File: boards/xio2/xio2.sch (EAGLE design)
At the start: 352 parts, among them J1 12401598E4#2A, Q1 BSS138, Q2 BSS138, Q3 BC817-16LT3G, Q4 BC817-16LT3G, Y2 FA-238 25.0000MB-K3

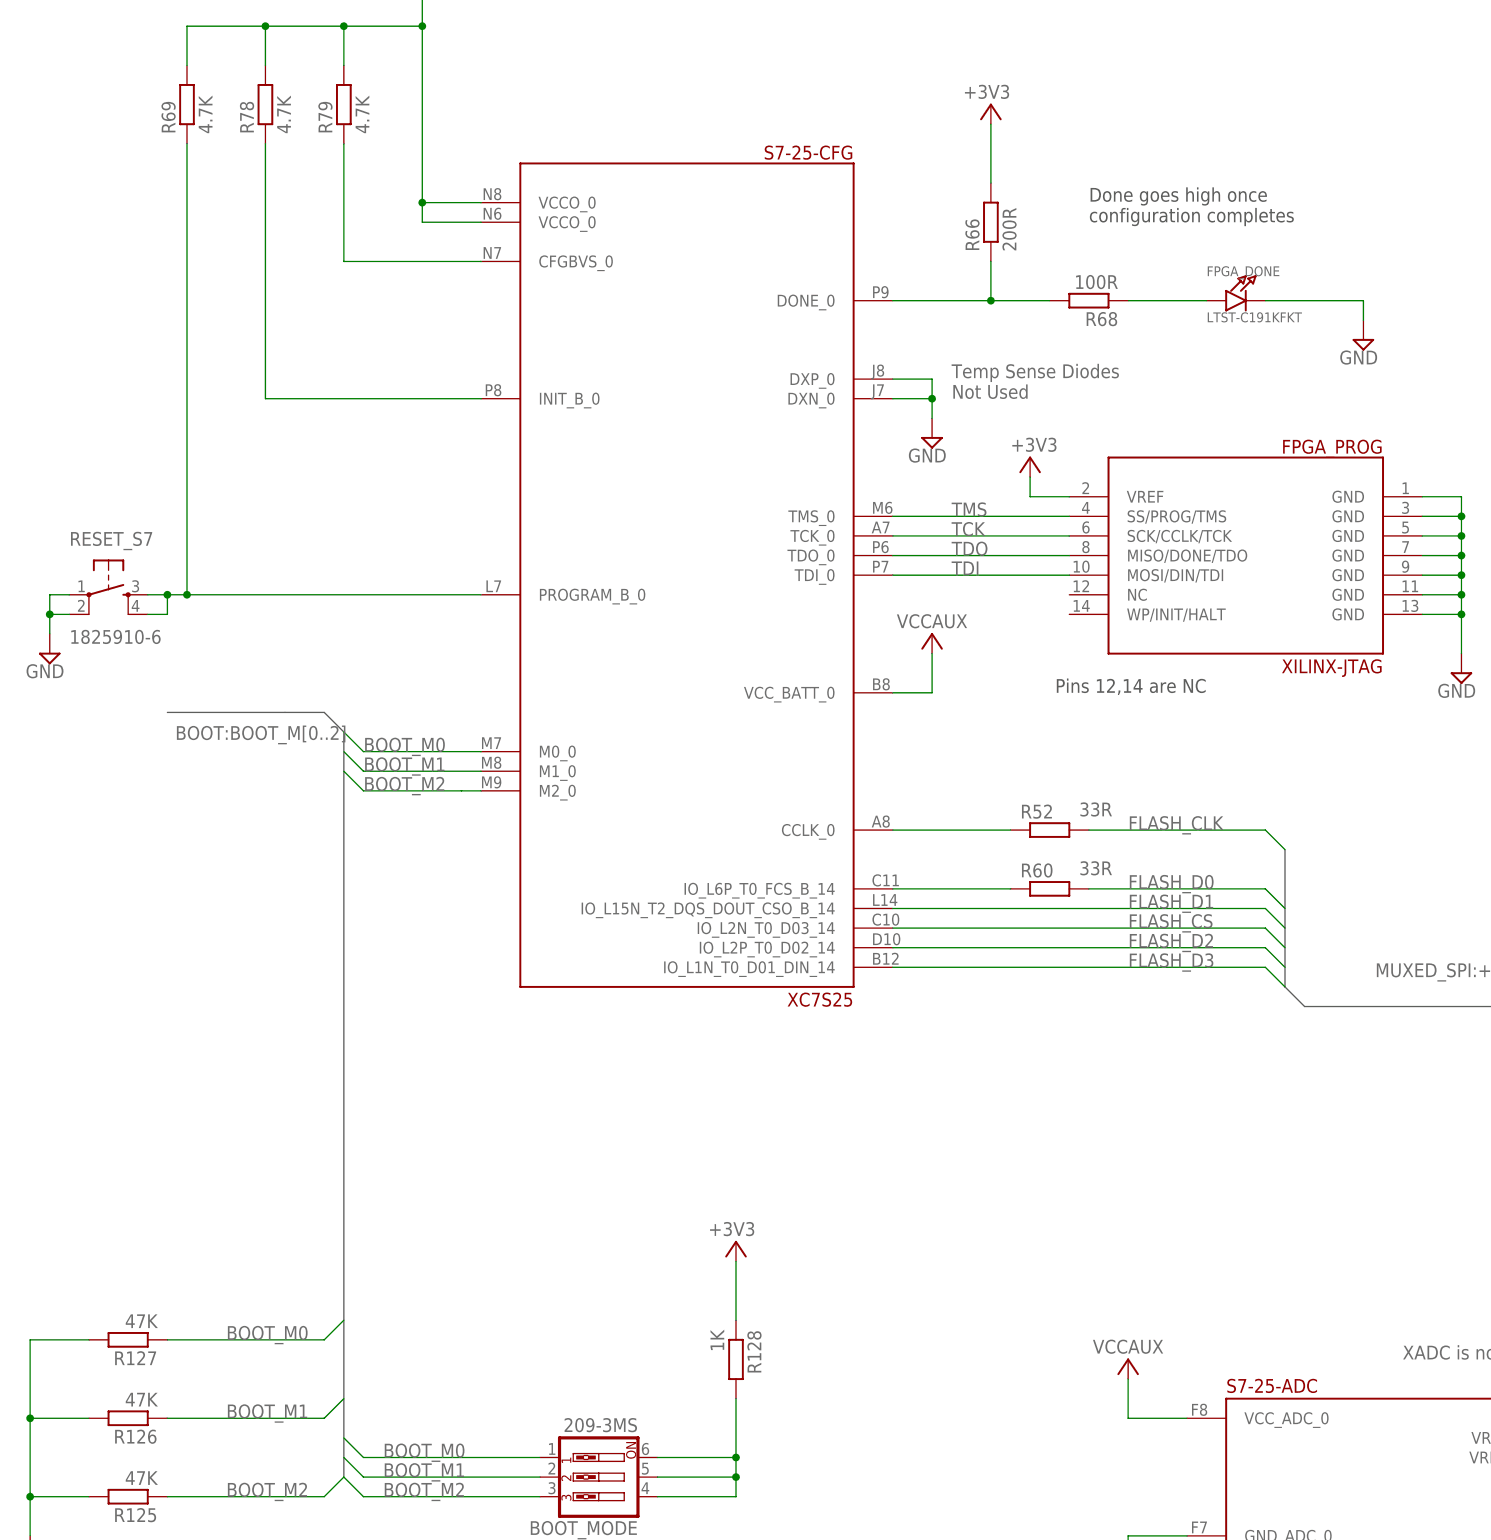
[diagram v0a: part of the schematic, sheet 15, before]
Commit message: All pins checked vs data sheets All parts provisionally given USE attributes
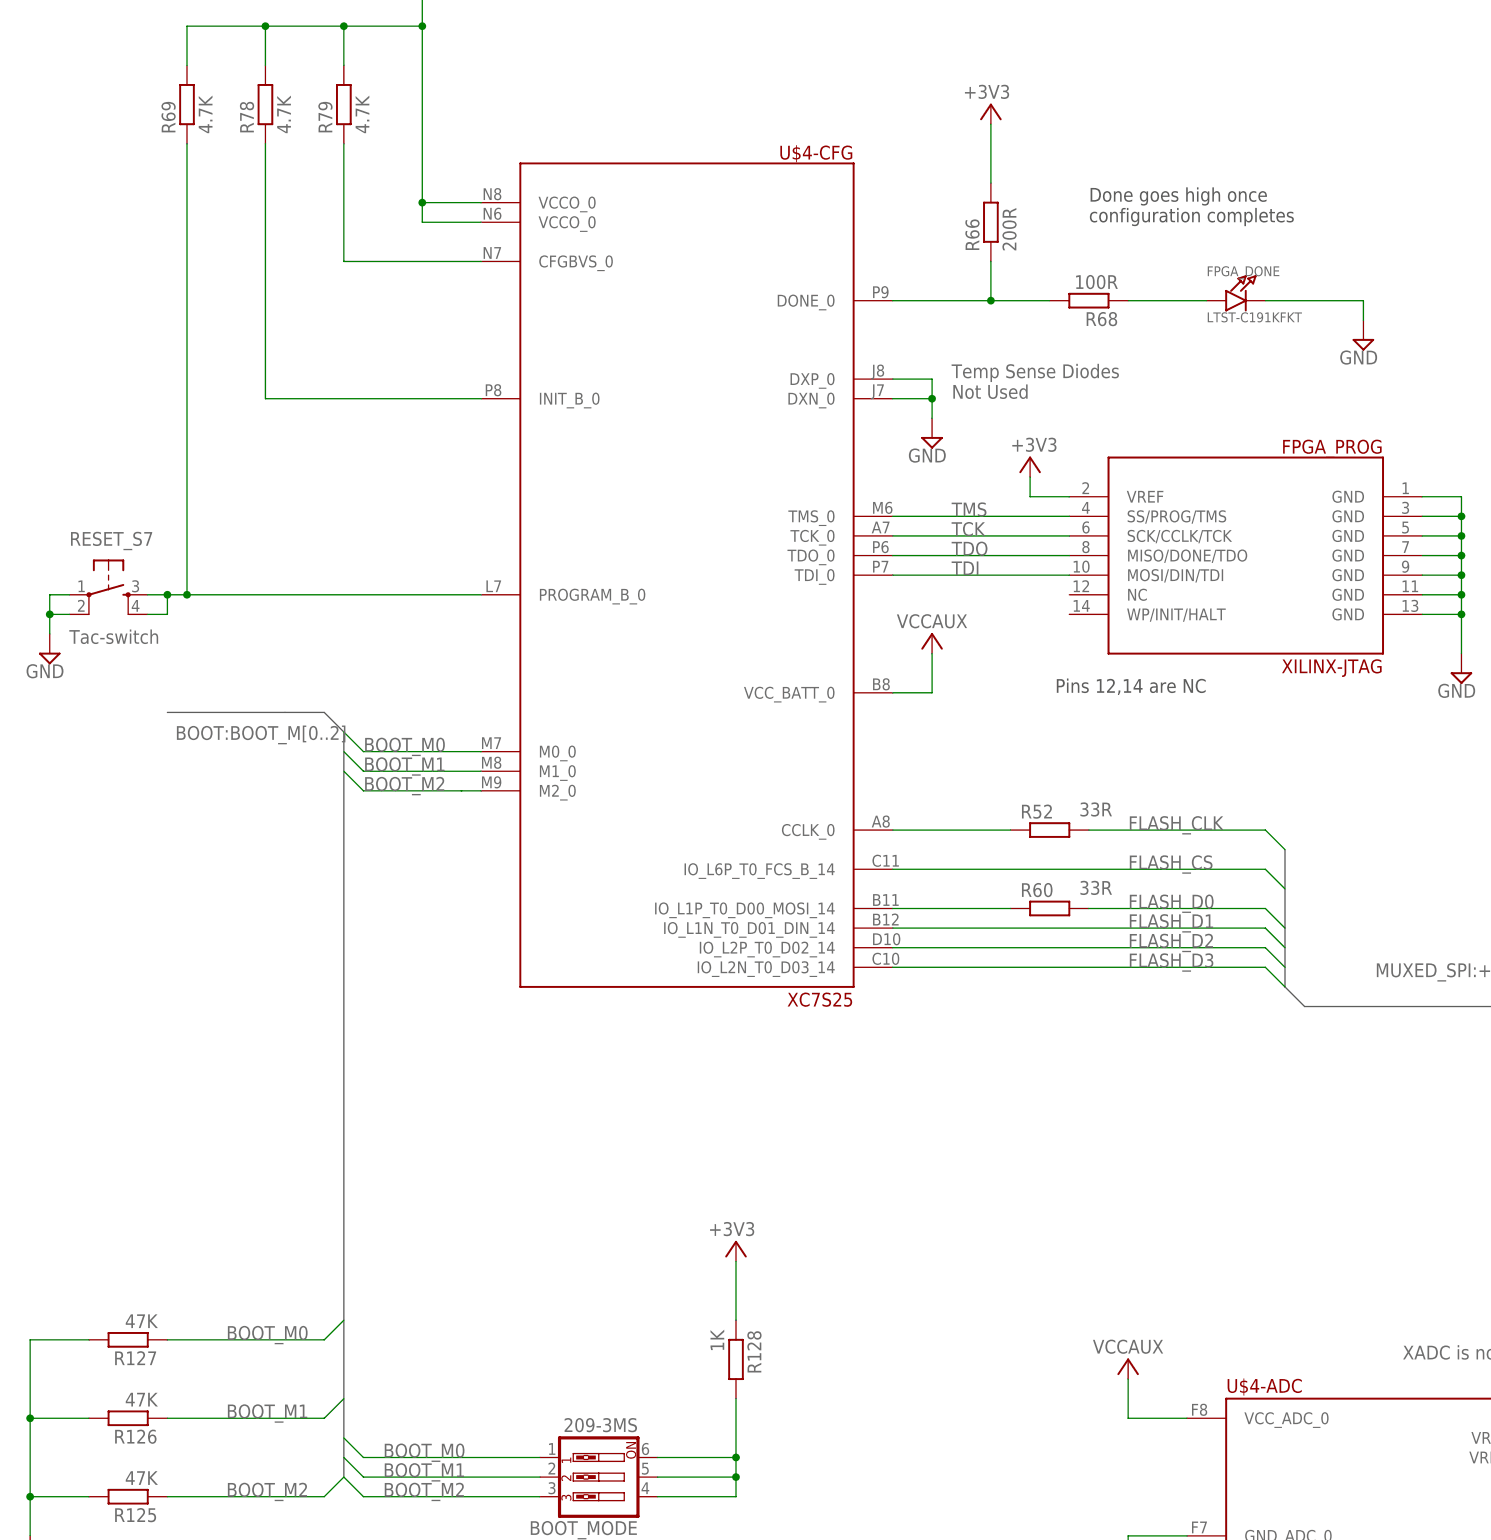
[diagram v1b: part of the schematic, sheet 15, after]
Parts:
- removed LVL_CLK, LVL_RD4, LVL_RD5, LVL_RW: 74LVCH1T45GW,125, sjg-logic:74LVC1T45GW,125
- added R58: 1K, rcl:R-EU_R0201
- added U$5, U$6, U$7, U$8: 74LVC1T45GWSOT866, sjg-logic:74LVC1T45GWSOT866
- A_MUX: USE (none) -> TS3A27518EPWR
- BOOT_MODE: USE (none) -> 209-3MS
- C100, C25, C57, C60, C61, C62, C63, C64, C65, C66, C67, C68, C69, C70, C71, C72, C88, C96: USE (none) -> GRM033R61A104ME15D
- C101, C73, C77: USE (none) -> GRM21BR60J107ME15L
- C102, C59, C74, C75, C76, C78, C79, C82: USE (none) -> GRM155R60J475ME87D
- C104, C30, C36, C47, C48, C49, C50, C51, C83, C84, C85, C86: USE (none) -> GRM033R60J474KE90D
- C109, C110: device rcl:C-EUC0603 -> rcl:C-EUC0805; USE (none) -> CL21A226MOCLRNC
- C111: USE (none) -> CL05B103KA5NNNC
- C112: USE (none) -> CL05B392KB5NNNC
- C35: value 0.01uF -> 0.1uF; USE (none) -> GRM033R61A104ME15D
- C52: USE (none) -> GRM21BR60J476ME15L
- C97: USE (none) -> GRM033R60J105MEA2D
- CARTRIDGE: USE (none) -> 5650118-1
- EXPANSION, EXP_POWER: NOSTUFF (none) -> true
- FPGA_1_0: USE (none) -> TLV62095RGTR
- FPGA_CFG: USE (none) -> MX25L3206EM2I-12G
- FPGA_DONE: UE (none) -> LTST-C191KFKT
- FPGA_PROG: USE (none) -> SBH21-NBPN-D07-ST-BK
- J1: USE (none) -> 12401598E4#2A
- L1: USE (none) -> ASPI-0530LR-1R5M-T2
- LD_0ACT, LD_1ACT, LD_2ACT, LD_3ACT, LD_4ACT: USE (none) -> 150060RS75000
- LD_0P, LD_1P, LD_2P, LD_3P, LD_4P: USE (none) -> SML-D12D1WT86
- LD_7DBG0, LD_7DBG1, LD_7DBG2: USE (none) -> ASMT-RA45-AP932
- LD_AUX, LD_INT, LD_V33: USE (none) -> LTST-S270GKT
- LVL_AHI, LVL_ALO, LVL_D: USE (none) -> SN74LVC8T245PWR
- MUX-HI, MUX-LO: USE (none) -> QS3VH257S1G
- OSC1: value ASEMB-50.000MHZ-LC-T -> 50 MHz oscillator; USE (none) -> SIT8008BI-23-33S-50.000000G
- Q3, Q4: USE (none) -> BC817-16LT3G
- R101, R104, R107, R87, R98: value 55R -> 59R; USE (none) -> RMCF0402FT59R0
- R102, R105, R108, R109, R110, R111, R94, R99: USE (none) -> RMCF0402JT130R
- R112: value 60R -> 59R; USE (none) -> RMCF0402FT59R0
- R113, R114, R115, R116, R117, R118: USE (none) -> RMCF0201FT49R9
- R125, R126, R127: USE (none) -> RMCF0402JT47K0
- R128: USE (none) -> RMCF0201JT1K00
- R129: USE (none) -> ERJ-2RKF4993X
- R130: USE (none) -> RMCF0402FT40K2
- R131: USE (none) -> RMCF0402JT160K
- R52, R60, R73, R74, R75: USE (none) -> RMCF0201JT33R0
- R54, R55, R57: USE (none) -> RC0603F242CS
- R66: USE (none) -> ERJ-1GNJ201C
- R67, R77: USE (none) -> RMCF0402JT150R
- R68: device rcl:R-EU_R0201 -> rcl:R-EU_R0402; USE (none) -> ERJ-2GEJ101X
- R69, R70, R71, R78, R79: USE (none) -> RC0603J472CS
- R76, R80: USE (none) -> RMCF0402JT330R
- RESET_S7: value 1825910-6 -> Tac-switch; USE (none) -> 1825910-6
- U$4: USE (none) -> XC7S25-2FTGB196I
- VREG_18: USE (none) -> TPS62087RLTR
- VREG_33: USE (none) -> LM21212MHX-2/NOPB
- XIO: USE (none) -> STM32H743XIH6
- renumbered S7-25 to U$4
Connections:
- removed net N$52: R60.1, U$4-CFG.IO_L6P_T0_FCS_B_14@C11
- new net N$3: R60.1, U$4-CFG.IO_L1P_T0_D00_MOSI_14@B11
- new net N$5: OSC1.INH, R58.2
- net +3V3: now also R58.1, U$5.DIR@5, U$5.VCCA@1, U$6.DIR@5, U$6.VCCA@1, U$7.VCCB@6, U$8.VCCB@6; no longer LVL_CLK.DIR@5, LVL_CLK.VCCA@1, LVL_RD4.VCCB@6, LVL_RD5.VCCB@6, LVL_RW.DIR@5, LVL_RW.VCCA@1
- net +5V: now also U$5.VCCB@6, U$6.VCCB@6, U$7.DIR@5, U$7.VCCA@1, U$8.DIR@5, U$8.VCCA@1; no longer LVL_CLK.VCCB@6, LVL_RD4.DIR@5, LVL_RD4.VCCA@1, LVL_RD5.DIR@5, LVL_RD5.VCCA@1, LVL_RW.VCCB@6
- net CART_CLK: now also U$5.B@4; no longer LVL_CLK.B@4
- net CART_R/!W!: now also U$6.B@4; no longer LVL_RW.B@4
- net CART_RD4: now also U$7.B@4; no longer LVL_RD4.B@4
- net CART_RD5: now also U$8.B@4; no longer LVL_RD5.B@4
- net FLASH_CS: now also U$4-CFG.IO_L6P_T0_FCS_B_14@C11; no longer U$4-CFG.IO_L2N_T0_D03_14@C10
- net FLASH_D1: now also U$4-CFG.IO_L1N_T0_D01_DIN_14@B12; no longer U$4-CFG.IO_L15N_T2_DQS_DOUT_CSO_B_14@L14
- net FLASH_D3: now also U$4-CFG.IO_L2N_T0_D03_14@C10; no longer U$4-CFG.IO_L1N_T0_D01_DIN_14@B12
- net GND: now also U$5.GND@2, U$6.GND@2, U$7.GND@2, U$8.GND@2; no longer LVL_CLK.GND@2, LVL_RD4.GND@2, LVL_RD5.GND@2, LVL_RW.GND@2
- net HOST_CLK: now also U$5.A@3; no longer LVL_CLK.A@3
- net HOST_R/!W!: now also U$4-BANK14.IO_L15N_T2_DQS_DOUT_CSO_B_14@L14, U$6.A@3; no longer LVL_RW.A@3, U$4-BANK14.IO_L1P_T0_D00_MOSI_14@B11
- net N$58: now also U$7.A@3; no longer LVL_RD4.A@3
- net N$59: now also U$8.A@3; no longer LVL_RD5.A@3
- net VCCAUX: now also VREG_18.NC@3
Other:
- note added: "TMDS_33 signalling requires 50R pull-ups to 3.3v on all inputs. Labels {RX*,TX*} are from perspective of the host board, so need to add pull-ups to TX* lines on this board. Will dissipate 13.5mA,"
- note removed: "ASPI-0530LR-1R5M-T2"
- note removed: "CL21A226MOCLRNC"
- note removed: "INH can be left floating for normal operation"
- note removed: "TMDS_33 signalling requires 50R pull-ups to 3.3v on all inputs. Labels {RX*,TX*} are from perspective of the host board, so need to add pull-ups to TX* lines on this board. Will dissipate 66mA, so need to be 0603"
- moved on the sheet: R60

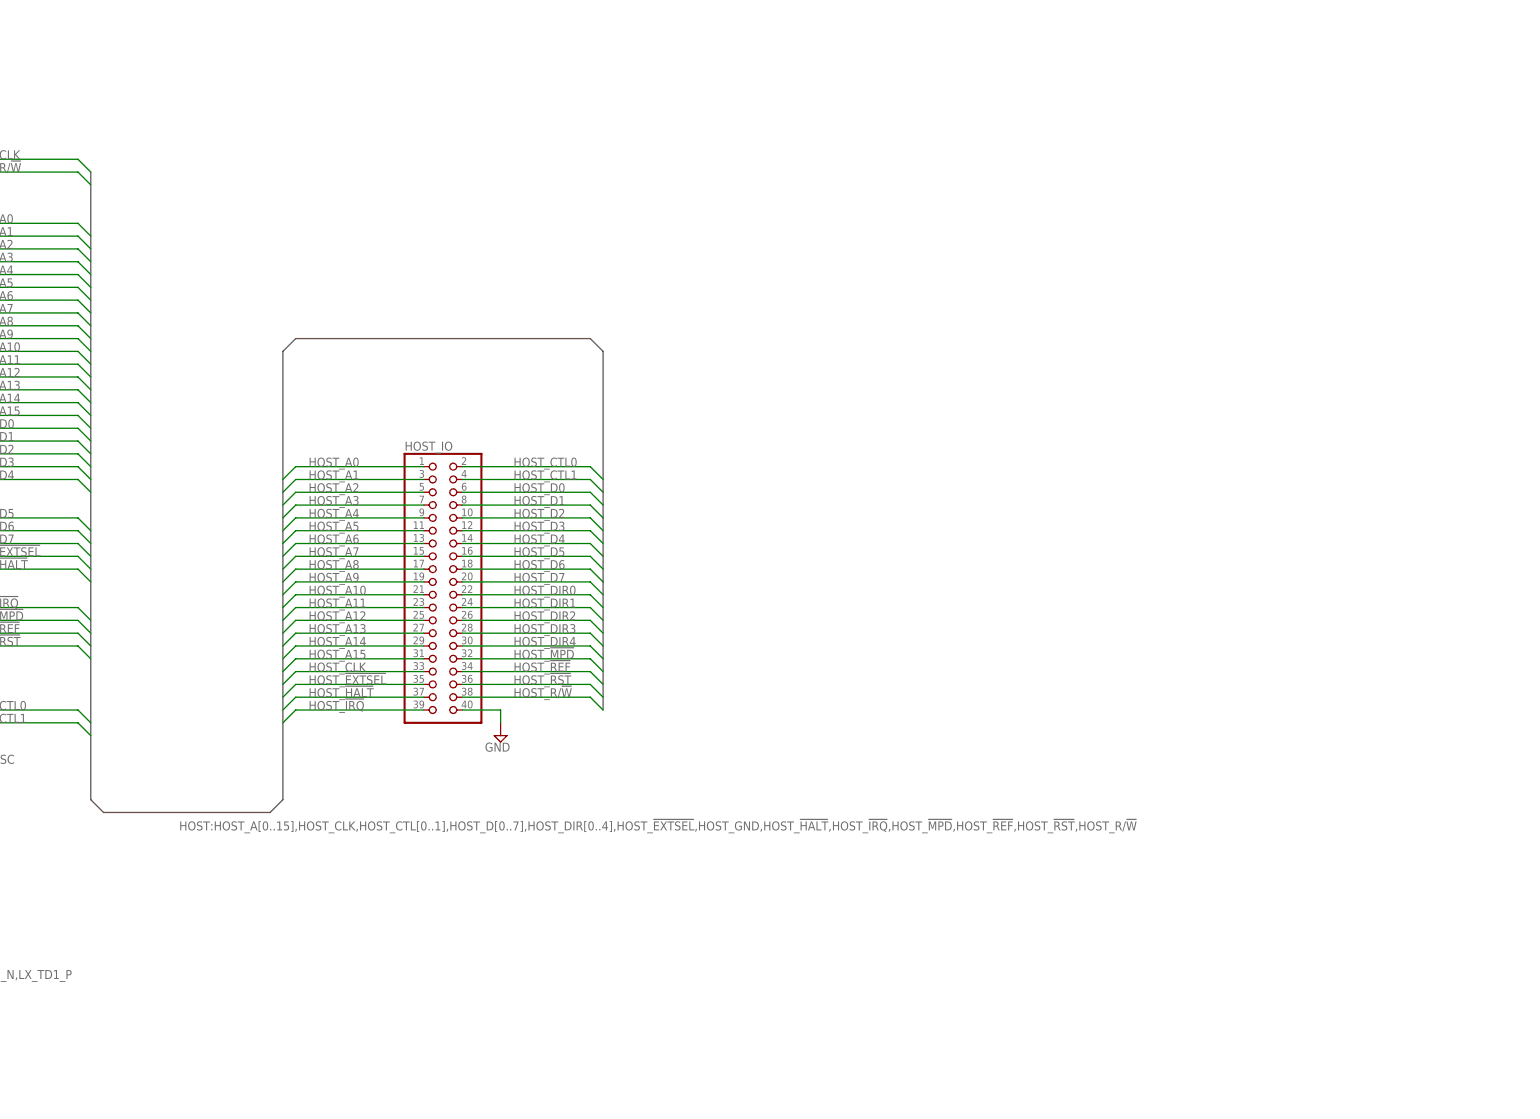
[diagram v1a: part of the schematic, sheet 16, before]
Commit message: Catch the last couple of cases where USE attributes or NOSTUFF attributes were not set
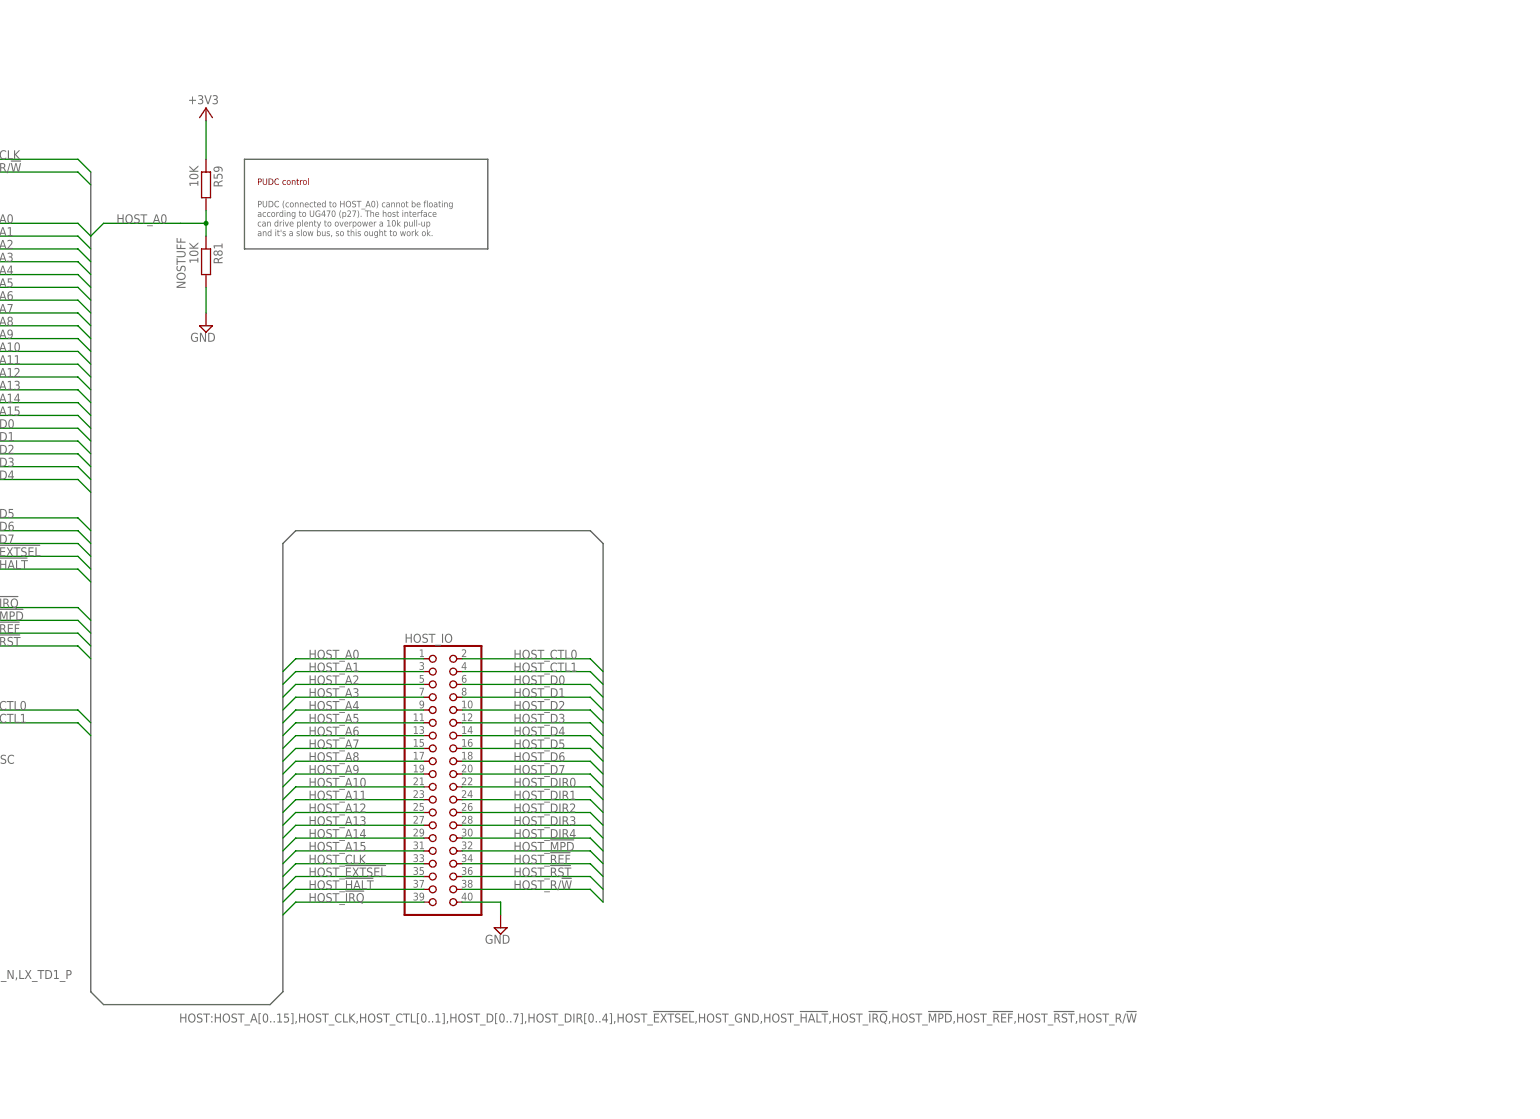
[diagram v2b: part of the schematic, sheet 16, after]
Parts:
- added R59, R81, R82, R83, R84, R85: 10K, rcl:R-EU_R0201
- C58: USE (none) -> GRM155R60J475ME87D
- FPGA_DONE: UE LTST-C191KFKT -> (none); USE (none) -> SML-D12D1WT86
- H1, H2, H4, H5, HOST_IO: NOSTUFF (none) -> true
- R61, R62, R63, R64, R65: USE (none) -> ERJ-1GNJ103C
- VREG_MON: USE (none) -> TPS3808G33DBVR
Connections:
- net +3V3: now also R59.1, R82.1, R83.1, R84.1, R85.1
- net GND: now also R81.2
- net HOST_A0: now also R59.2, R81.1
- net TCK: now also R83.2
- net TDI: now also R85.2
- net TDO: now also R84.2
- net TMS: now also R82.2
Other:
- note added: "PUDC (connected to HOST_A0) cannot be floating according to UG470 (p27). The host interface can drive plenty to overpower a 10k pull-up and it's a slow bus, so this ought to work ok."
- note added: "PUDC control"
- moved on the sheet: HOST_IO, R68

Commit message: Add a facility for external power
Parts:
- added PEXT_10, PEXT_18: (no value), pinhead:PINHD-1X2
- added PEXT_33: (no value), pinhead:PINHD-2X2
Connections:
- net +3V3: now also PEXT_33.1, PEXT_33.2, PEXT_33.3, PEXT_33.4
- net VCCAUX: now also PEXT_18.1, PEXT_18.2
- net VCCINT: now also PEXT_10.1, PEXT_10.2
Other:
- moved on the sheet: C101, C102, C104, C30, C36, C47, C48, C49, C50, C51, C52, C58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
